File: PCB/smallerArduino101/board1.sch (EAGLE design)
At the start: 43 parts

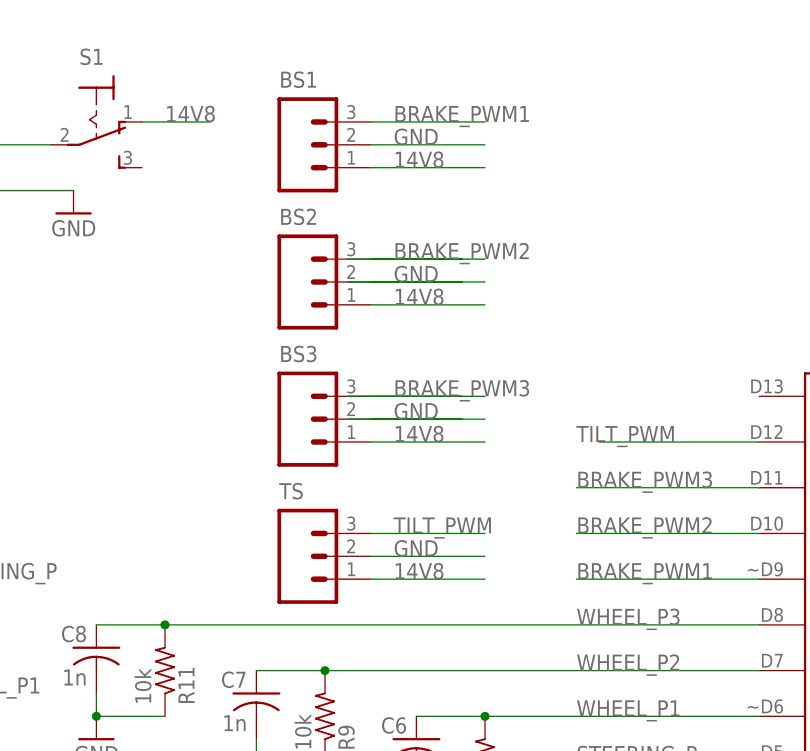
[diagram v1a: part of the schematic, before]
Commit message: v2 pcb, code for pid, data for pid on bike
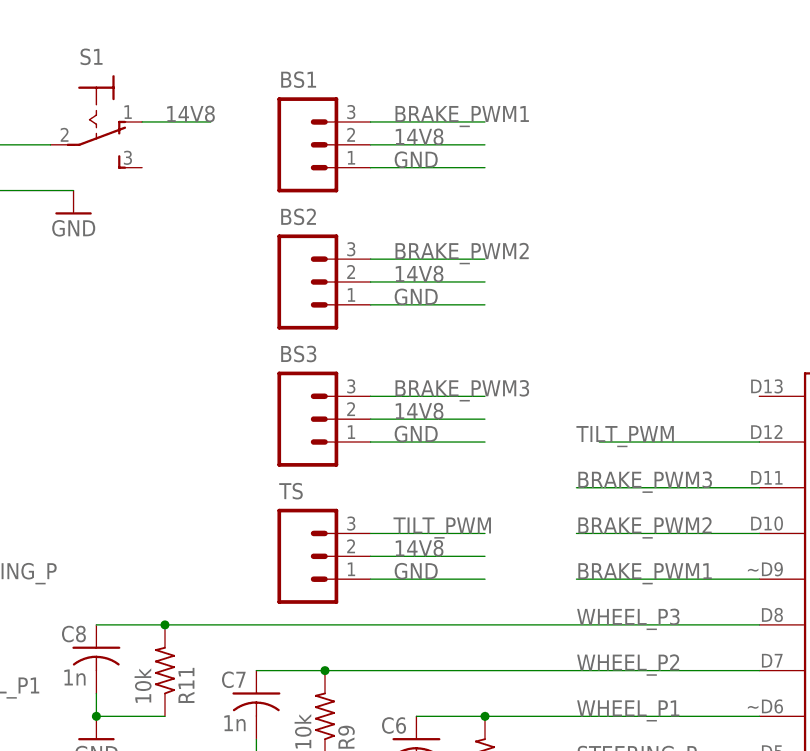
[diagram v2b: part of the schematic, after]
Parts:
- S1: device switch:320-916 -> switch:M9040P
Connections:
- net 14V8: now also BS1.2, BS2.2, BS3.2, TS.2; no longer BS1.1, BS2.1, BS3.1, TS.1
- net GND: now also BS1.1, BS2.1, BS3.1, TS.1; no longer BS1.2, BS2.2, BS3.2, TS.2
